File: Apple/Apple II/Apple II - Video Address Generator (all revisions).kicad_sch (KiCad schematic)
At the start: 0 parts

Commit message: Finished Apple II Sheet 3 of 23: Video Address Generator (all revisions)
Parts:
- added J?: Conn_01x04_Male, symbol Connector:Conn_01x04_Male
- added JP15: 15, symbol Jumper:SolderJumper_2_Open
- added N1 (x2): 1, symbol Apple II:NOTE_NUMBER
- added N2 (x2): 2, symbol Apple II:NOTE_NUMBER
- added N3 (x2): 3, symbol Apple II:NOTE_NUMBER
- added N4 (x2): 4, symbol Apple II:NOTE_NUMBER
- added O? (x5): SOFT_5, symbol Apple II:SOFT_5
- added RA02: 1K, Resistor_THT:R_Array_SIP9, symbol Device:R_Network08_Split
- added U?: D11_74LS161, symbol Apple II:D11_74LS161
- added U?: 74LS04, symbol Apple II:C11_74LS04
- added U?: D14_74LS161, symbol Apple II:D14_74LS161
- added U?: D13_74LS161, symbol Apple II:D13_74LS161
- added U?: D12_74LS161, symbol Apple II:D12_74LS161
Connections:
- new net: O?., U?.1 (~{CLR}) (x2)
- new net: U?.10 (ET), U?.15 (RC), U?.4 (P1), U?.5 (P2), U?.7 (EP)
- new net: U?.15 (RC), U?.9
- new net: JP15.2 (B), RA02.2 (R1.2), U?.3 (P0), U?.3 (P0), U?.6 (P3)
- new net: U?.8, U?.9 (~{PE})
- new net: O?., U?.1 (~{CLR}), U?.10 (ET), U?.7 (EP)
- new net: J?.3 (Pin_3), O?.
- new net: J?.4 (Pin_4), U?.9 (~{PE})
- new net: U?.10 (ET), U?.15 (RC), U?.7 (EP)
- new net: O?., U?.1 (~{CLR}), U?.5 (P2)
- new net: U?.10 (ET), U?.15 (RC), U?.5 (P2), U?.7 (EP)
- new net +5V: RA02.1 (R1.1)
- new net 14M: J?.2 (Pin_2)
- new net Earth: J?.1 (Pin_1), JP15.1 (A), U?.3 (P0), U?.3 (P0), U?.4 (P1), U?.4 (P1), U?.4 (P1), U?.5 (P2), U?.6 (P3), U?.6 (P3)
- new net H0: U?.14 (Q0)
- new net H1: U?.13 (Q1)
- new net H2: U?.12 (Q2)
- new net H3: U?.11 (Q3)
- new net H4: U?.14 (Q0)
- new net H5: U?.13 (Q1)
- new net V0: U?.12 (Q2)
- new net V1: U?.11 (Q3)
- new net V2: U?.14 (Q0)
- new net V3: U?.13 (Q1)
- new net V4: U?.12 (Q2)
- new net V5: U?.11 (Q3)
- new net VA: U?.11 (Q3), U?.6 (P3)
- new net VB: U?.14 (Q0)
- new net VC: U?.13 (Q1)
- new net ~{HPE}: U?.12 (Q2), U?.9 (~{PE}), U?.9 (~{PE})
- new net ~{LDPS}: U?.2 (CP), U?.2 (CP), U?.2 (CP), U?.2 (CP)
- no-connect marks 0 -> 2
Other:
- note added: "CIRCUIT FOR REV. 0"
- note added: "CIRCUIT FOR REV. 1,7,RFI"
- note added: "D11-11 NOT CONNECTED ON REV. 0"
- note added: "HORIZONTAL VIDEO ADDRESS"
- note added: "NC"
- note added: "TEST CONNECTOR NEAR B2 ON SOME RFI BOARDS. A SIMILAR CONNECTOR WITH DIFFERENT CONNECTIONS MAY APPEAR ON REV. 7 BOARDS."
- note added: "TO CLOCK GENERATOR"
- note added: "VERTICAL VIDEO ADDRESS"
- title: (none) -> Apple II - Video Address Generator

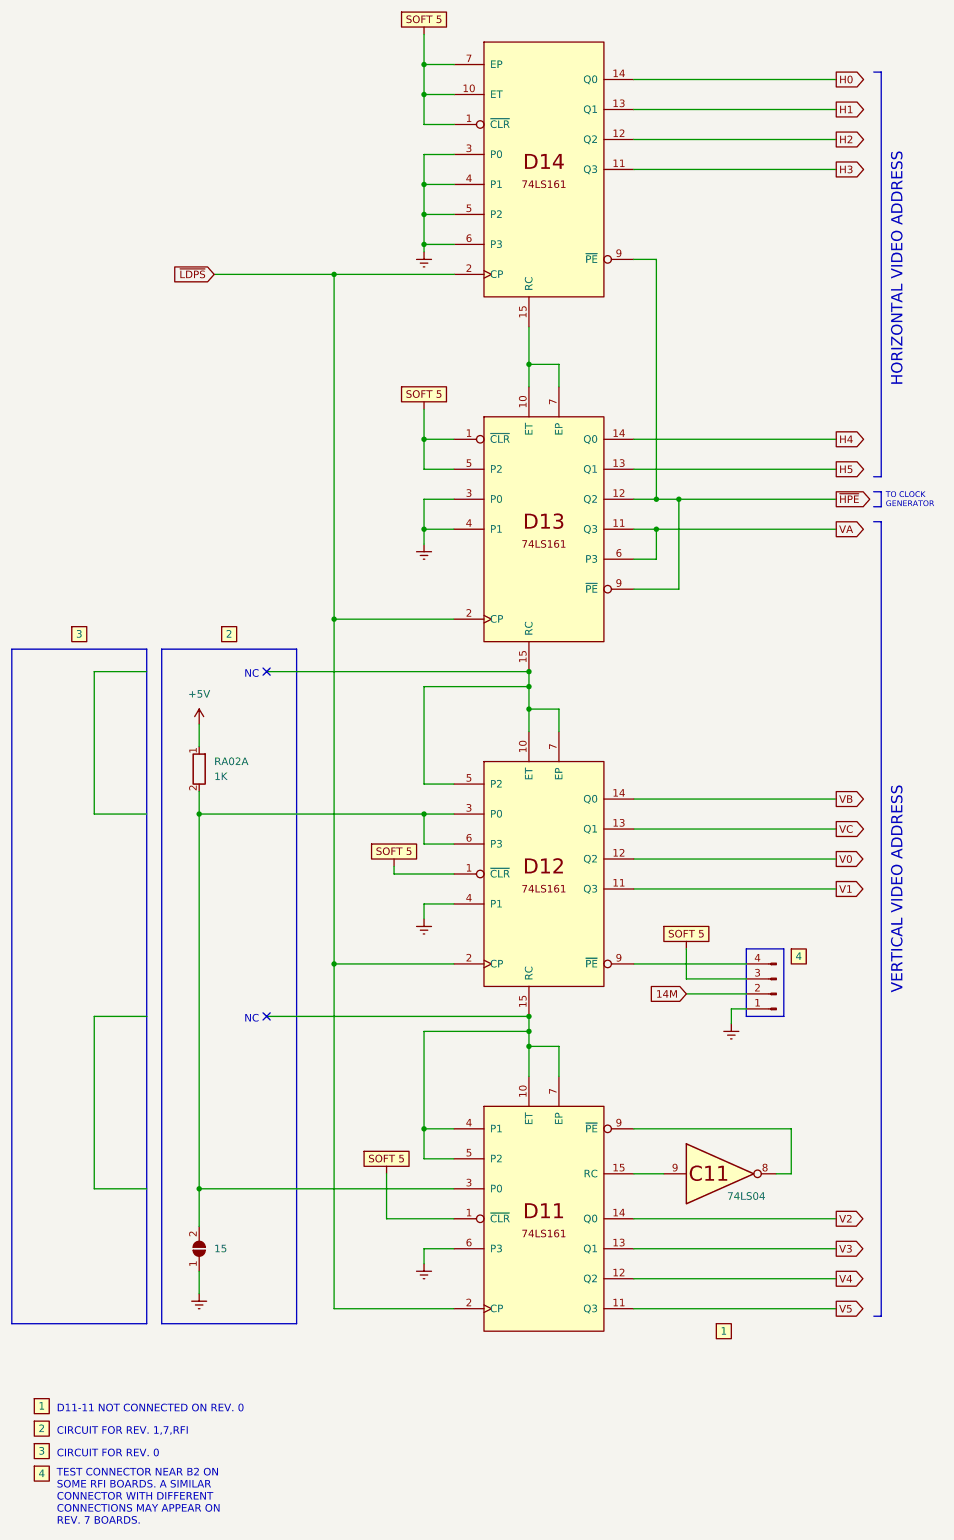
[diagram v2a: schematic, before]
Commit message: Finished Apple II - Sheet 6 - Memory Address Pt 2 of 2 (All Revisions)
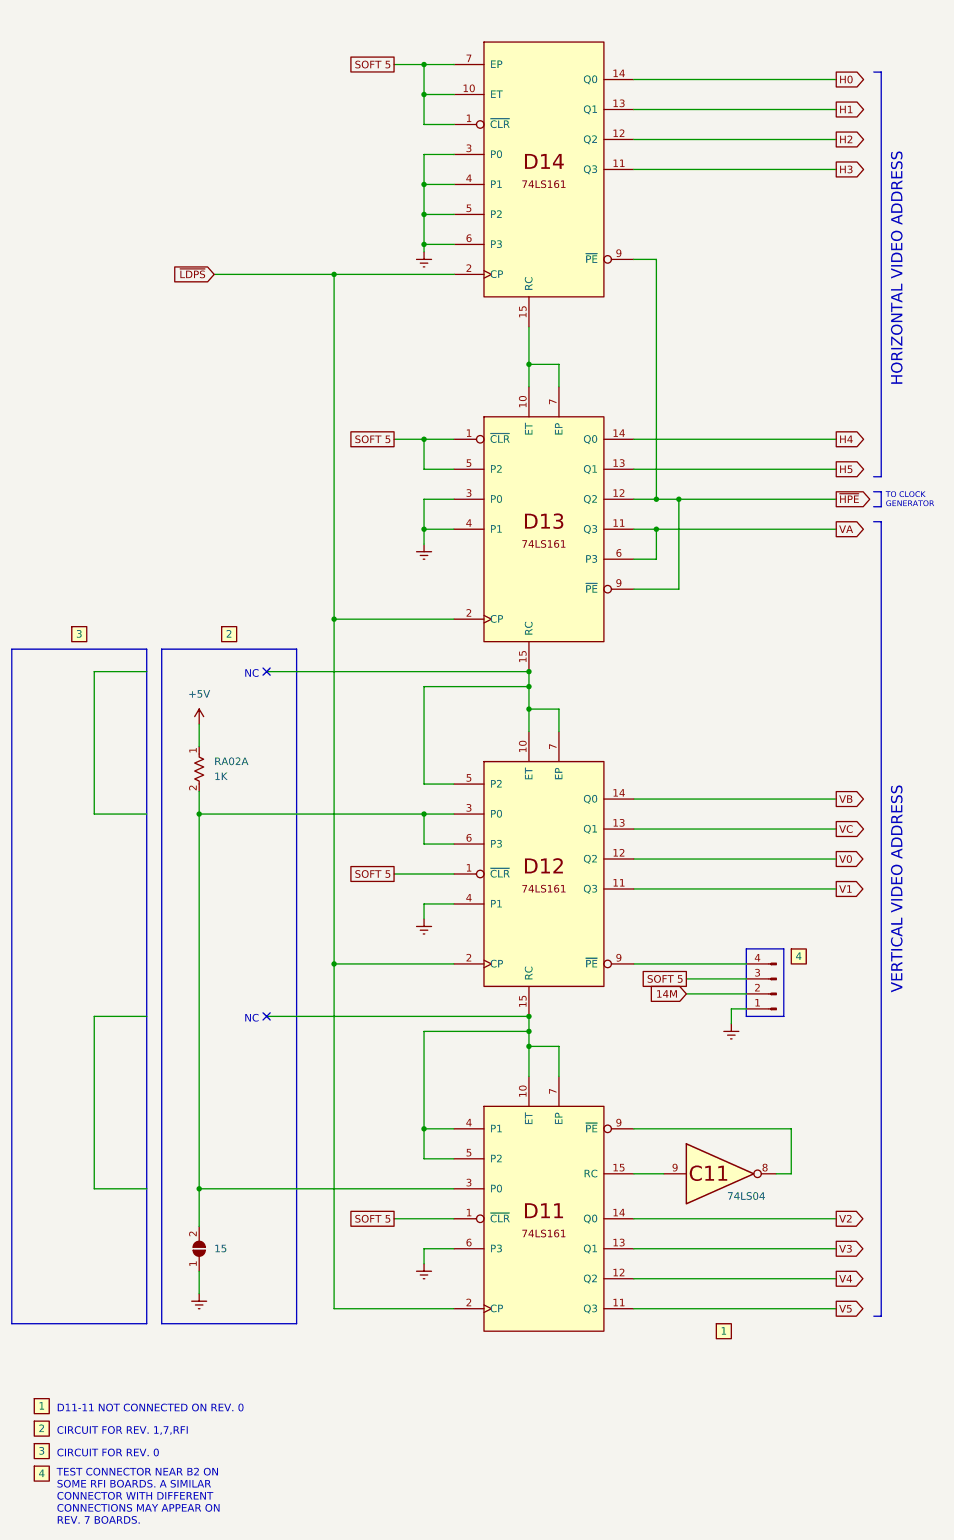
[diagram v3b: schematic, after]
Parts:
- removed O? (x5): SOFT_5, symbol Apple II:SOFT_5
- RA02: symbol Device:R_Network08_Split -> Apple II:R_Network08_US_Split
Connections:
- net SOFT 5: now reaches U?.1 (~{CLR})
- net SOFT 5: now also J?.3 (Pin_3), U?.1 (~{CLR}), U?.1 (~{CLR}), U?.1 (~{CLR}), U?.10 (ET), U?.5 (P2), U?.7 (EP)
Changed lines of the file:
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@@
   (junction (at 114.3 129.54) (diameter 0) (color 0 0 0 0)
   )
+  (junction (at 96.52 26.67) (diameter 0) (color 0 0 0 0)
+  )
   (junction (at 96.52 153.67) (diameter 0) (color 0 0 0 0)
   )
@@
   )
   (junction (at 114.3 193.04) (diameter 0) (color 0 0 0 0)
-  )
-  (junction (at 96.52 26.67) (diameter 0) (color 0 0 0 0)
   )
   (junction (at 96.52 46.99) (diameter 0) (color 0 0 0 0)
@@
     (stroke (width 0) (type default) (color 0 0 0 0))
   )
-  (wire (pts (xy 101.6 222.25) (xy 90.17 222.25))
+  (wire (pts (xy 101.6 222.25) (xy 91.44 222.25))
     (stroke (width 0) (type default) (color 0 0 0 0))
   )
@@
     (stroke (width 0) (type solid) (color 0 0 0 0))
   )
-  (wire (pts (xy 140.97 181.61) (xy 140.97 176.53))
-    (stroke (width 0) (type default) (color 0 0 0 0))
-  )
   (wire (pts (xy 114.3 193.04) (xy 114.3 198.12))
     (stroke (width 0) (type default) (color 0 0 0 0))
@@
   )
   (wire (pts (xy 158.75 207.01) (xy 158.75 214.63))
-    (stroke (width 0) (type default) (color 0 0 0 0))
-  )
-  (wire (pts (xy 96.52 21.59) (xy 96.52 26.67))
     (stroke (width 0) (type default) (color 0 0 0 0))
   )
@@
     (stroke (width 0) (type default) (color 0 0 0 0))
   )
+  (wire (pts (xy 91.44 26.67) (xy 96.52 26.67))
+    (stroke (width 0) (type default) (color 0 0 0 0))
+  )
   (wire (pts (xy 166.37 232.41) (xy 132.08 232.41))
     (stroke (width 0) (type default) (color 0 0 0 0))
@@
   )
   (wire (pts (xy 101.6 158.75) (xy 96.52 158.75))
-    (stroke (width 0) (type default) (color 0 0 0 0))
-  )
-  (wire (pts (xy 91.44 163.83) (xy 91.44 162.56))
     (stroke (width 0) (type default) (color 0 0 0 0))
   )
@@
     (stroke (width 0) (type default) (color 0 0 0 0))
   )
-  (wire (pts (xy 96.52 85.09) (xy 96.52 90.17))
-    (stroke (width 0) (type default) (color 0 0 0 0))
-  )
-  (wire (pts (xy 90.17 222.25) (xy 90.17 214.63))
+  (wire (pts (xy 91.44 90.17) (xy 96.52 90.17))
     (stroke (width 0) (type default) (color 0 0 0 0))
   )
@@
     )
   )
+  (global_label "SOFT 5" (shape passive) (at 91.44 90.17 180) (fields_autoplaced)
+    (effects (font (size 1.27 1.27)) (justify right))
+    (property "Intersheet References" "${INTERSHEET_REFS}" (id 0) (at 82.2536 90.0906 0)
+      (effects (font (size 1.27 1.27)) (justify right) hide)
+    )
+  )
   (global_label "~{LDPS}" (shape input) (at 60.96 62.23 180) (fields_autoplaced)
     (effects (font (size 1.27 1.27)) (justify right))
@@
     )
   )
+  (global_label "SOFT 5" (shape passive) (at 91.44 26.67 180) (fields_autoplaced)
+    (effects (font (size 1.27 1.27)) (justify right))
+    (property "Intersheet References" "${INTERSHEET_REFS}" (id 0) (at 82.2536 26.5906 0)
+      (effects (font (size 1.27 1.27)) (justify right) hide)
+    )
+  )
+  (global_label "SOFT 5" (shape passive) (at 140.97 181.61 180) (fields_autoplaced)
+    (effects (font (size 1.27 1.27)) (justify right))
+    (property "Intersheet References" "${INTERSHEET_REFS}" (id 0) (at 131.7836 181.5306 0)
+      (effects (font (size 1.27 1.27)) (justify right) hide)
+    )
+  )
+  (global_label "SOFT 5" (shape passive) (at 91.44 163.83 180) (fields_autoplaced)
+    (effects (font (size 1.27 1.27)) (justify right))
+    (property "Intersheet References" "${INTERSHEET_REFS}" (id 0) (at 82.2536 163.7506 0)
+      (effects (font (size 1.27 1.27)) (justify right) hide)
+    )
+  )
   (global_label "H4" (shape output) (at 166.37 90.17 0) (fields_autoplaced)
     (effects (font (size 1.27 1.27)) (justify left))
@@
     (property "Intersheet References" "${INTERSHEET_REFS}" (id 0) (at 171.3231 39.2906 0)
       (effects (font (size 1.27 1.27)) (justify left) hide)
+    )
+  )
+  (global_label "SOFT 5" (shape passive) (at 91.44 222.25 180) (fields_autoplaced)
+    (effects (font (size 1.27 1.27)) (justify right))
+    (property "Intersheet References" "${INTERSHEET_REFS}" (id 0) (at 82.2536 222.1706 0)
+      (effects (font (size 1.27 1.27)) (justify right) hide)
     )
   )
@@
       (effects (font (size 1.27 1.27)) hide)
     )
-  )
-  (symbol (lib_id "Apple II:SOFT_5") (at 90.17 212.09 0) (unit 1)
-    (in_bom yes) (on_board yes) (fields_autoplaced)
-    (property "Reference" "O?" (id 0) (at 68.58 195.58 0)
-      (effects (font (size 1.27 1.27)) hide)
-    )
-    (property "Value" "SOFT_5" (id 1) (at 68.58 198.12 0)
-      (effects (font (size 1.27 1.27)) hide)
-    )
-    (property "Footprint" "" (id 2) (at 68.58 195.58 0)
-      (effects (font (size 1.27 1.27)) hide)
-    )
-    (property "Datasheet" "" (id 3) (at 68.58 195.58 0)
-      (effects (font (size 1.27 1.27)) hide)
-    )
-    (pin "")
   )
   (symbol (lib_id "Apple II:D11_74LS161") (at 106.68 203.2 0) (unit 1)
@@
     )
   )
-  (symbol (lib_id "Device:R_Network08_Split") (at 58.42 146.05 0) (unit 1)
+  (symbol (lib_id "Apple II:R_Network08_US_Split") (at 58.42 146.05 0) (unit 1)
     (in_bom yes) (on_board yes) (fields_autoplaced)
     (property "Reference" "RA02" (id 0) (at 60.96 144.7799 0)
@@
       (effects (font (size 1.27 1.27)) (justify left))
     )
-    (property "Footprint" "Resistor_THT:R_Array_SIP9" (id 2) (at 56.388 146.05 90)
-      (effects (font (size 1.27 1.27)) hide)
-    )
-    (property "Datasheet" "http://www.vishay.com/docs/31509/csc.pdf" (id 3) (at 58.42 146.05 0)
+    (property "Footprint" "Resistor_THT:R_Array_SIP9" (id 2) (at 14.224 123.444 90)
+      (effects (font (size 1.27 1.27)) hide)
+    )
+    (property "Datasheet" "http://www.vishay.com/docs/31509/csc.pdf" (id 3) (at 13.97 122.682 0)
       (effects (font (size 1.27 1.27)) hide)
     )
@@
     (pin "13")
   )
-  (symbol (lib_id "Apple II:SOFT_5") (at 91.44 160.02 0) (unit 1)
-    (in_bom yes) (on_board yes) (fields_autoplaced)
-    (property "Reference" "O?" (id 0) (at 69.85 143.51 0)
-      (effects (font (size 1.27 1.27)) hide)
-    )
-    (property "Value" "SOFT_5" (id 1) (at 69.85 146.05 0)
-      (effects (font (size 1.27 1.27)) hide)
-    )
-    (property "Footprint" "" (id 2) (at 69.85 143.51 0)
-      (effects (font (size 1.27 1.27)) hide)
-    )
-    (property "Datasheet" "" (id 3) (at 69.85 143.51 0)
-      (effects (font (size 1.27 1.27)) hide)
-    )
-    (pin "")
-  )
   (symbol (lib_id "Apple II:NOTE_NUMBER") (at 63.5 123.19 0) (unit 1)
     (in_bom yes) (on_board yes)
@@
       (effects (font (size 1.27 1.27)) hide)
     )
-  )
-  (symbol (lib_id "Apple II:SOFT_5") (at 96.52 19.05 0) (unit 1)
-    (in_bom yes) (on_board yes) (fields_autoplaced)
-    (property "Reference" "O?" (id 0) (at 74.93 2.54 0)
-      (effects (font (size 1.27 1.27)) hide)
-    )
-    (property "Value" "SOFT_5" (id 1) (at 74.93 5.08 0)
-      (effects (font (size 1.27 1.27)) hide)
-    )
-    (property "Footprint" "" (id 2) (at 74.93 2.54 0)
-      (effects (font (size 1.27 1.27)) hide)
-    )
-    (property "Datasheet" "" (id 3) (at 74.93 2.54 0)
-      (effects (font (size 1.27 1.27)) hide)
-    )
-    (pin "")
   )
   (symbol (lib_id "Connector:Conn_01x04_Male") (at 156.21 184.15 180) (unit 1)
@@
     (pin "1")
     (pin "2")
-  )
-  (symbol (lib_id "Apple II:SOFT_5") (at 140.97 173.99 0) (unit 1)
-    (in_bom yes) (on_board yes) (fields_autoplaced)
-    (property "Reference" "O?" (id 0) (at 119.38 157.48 0)
-      (effects (font (size 1.27 1.27)) hide)
-    )
-    (property "Value" "SOFT_5" (id 1) (at 119.38 160.02 0)
-      (effects (font (size 1.27 1.27)) hide)
-    )
-    (property "Footprint" "" (id 2) (at 119.38 157.48 0)
-      (effects (font (size 1.27 1.27)) hide)
-    )
-    (property "Datasheet" "" (id 3) (at 119.38 157.48 0)
-      (effects (font (size 1.27 1.27)) hide)
-    )
-    (pin "")
   )
   (symbol (lib_id "power:Earth") (at 96.52 58.42 0) (unit 1)
@@
     )
   )
-  (symbol (lib_id "Apple II:SOFT_5") (at 96.52 82.55 0) (unit 1)
-    (in_bom yes) (on_board yes) (fields_autoplaced)
-    (property "Reference" "O?" (id 0) (at 74.93 66.04 0)
-      (effects (font (size 1.27 1.27)) hide)
-    )
-    (property "Value" "SOFT_5" (id 1) (at 74.93 68.58 0)
-      (effects (font (size 1.27 1.27)) hide)
-    )
-    (property "Footprint" "" (id 2) (at 74.93 66.04 0)
-      (effects (font (size 1.27 1.27)) hide)
-    )
-    (property "Datasheet" "" (id 3) (at 74.93 66.04 0)
-      (effects (font (size 1.27 1.27)) hide)
-    )
-    (pin "")
-  )
   (symbol (lib_id "power:+5V") (at 58.42 138.43 0) (unit 1)
